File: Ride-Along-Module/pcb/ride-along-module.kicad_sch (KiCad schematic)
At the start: 7 parts

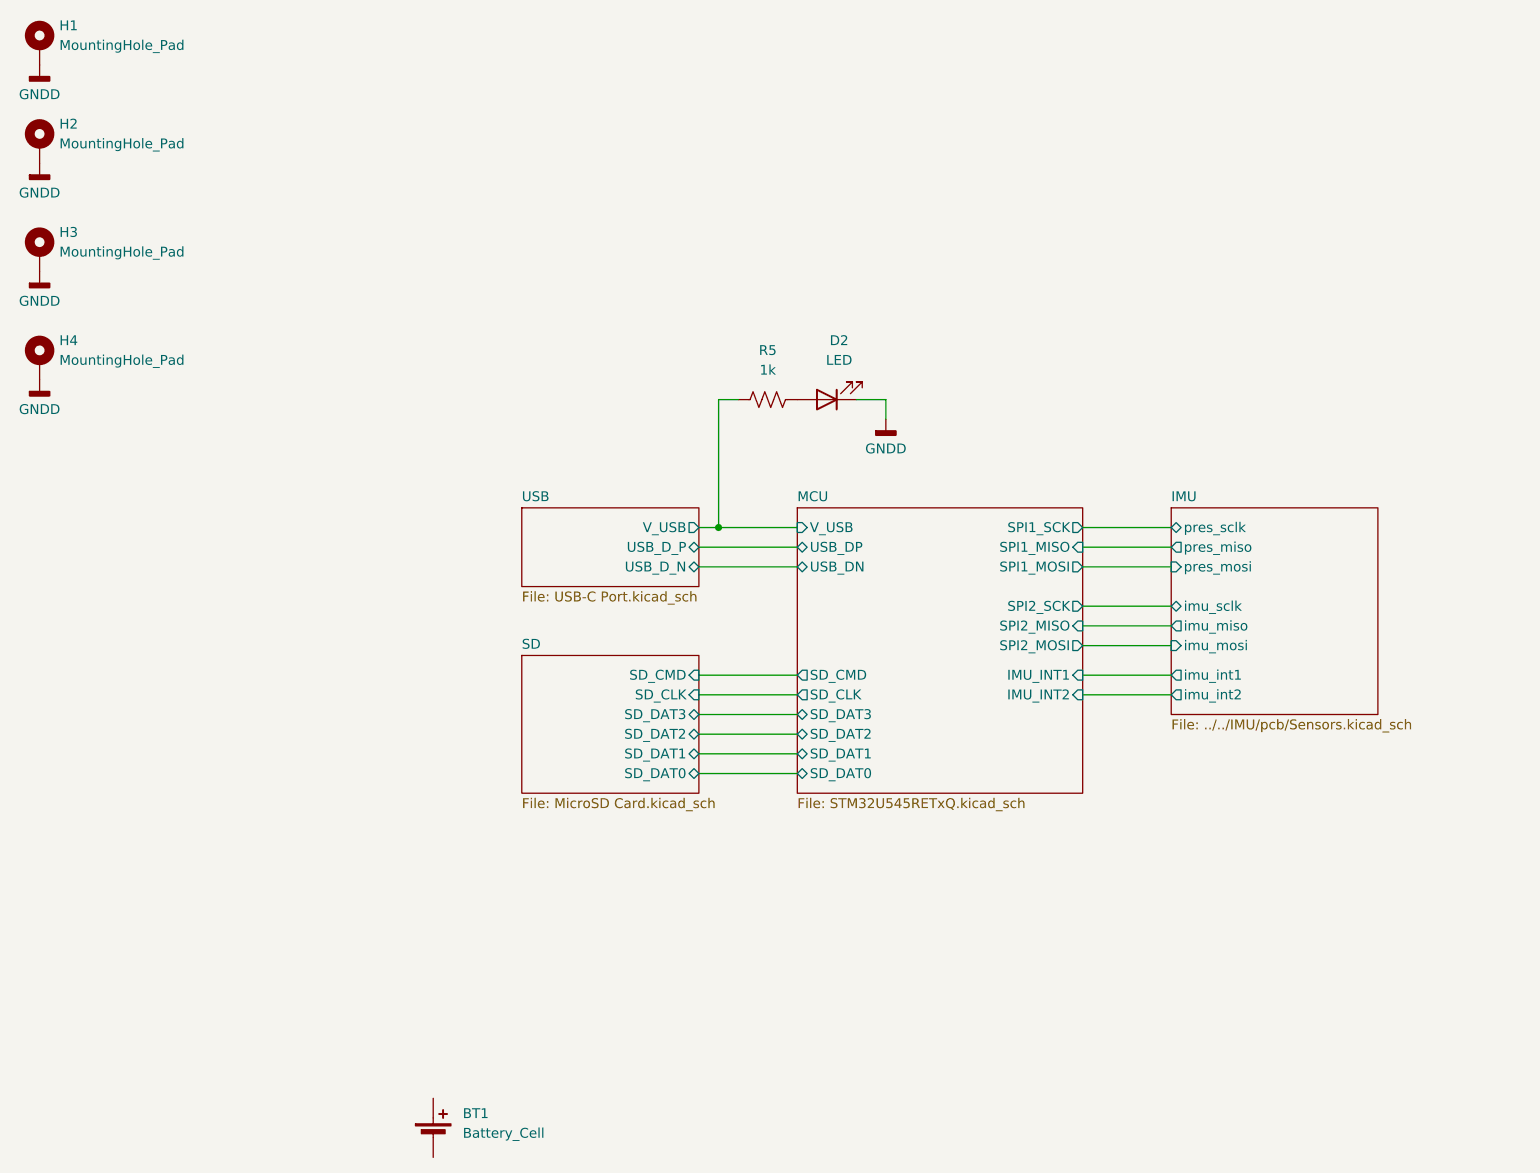
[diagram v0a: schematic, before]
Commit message: More reuse blocks. Added battery circuit to ride along board
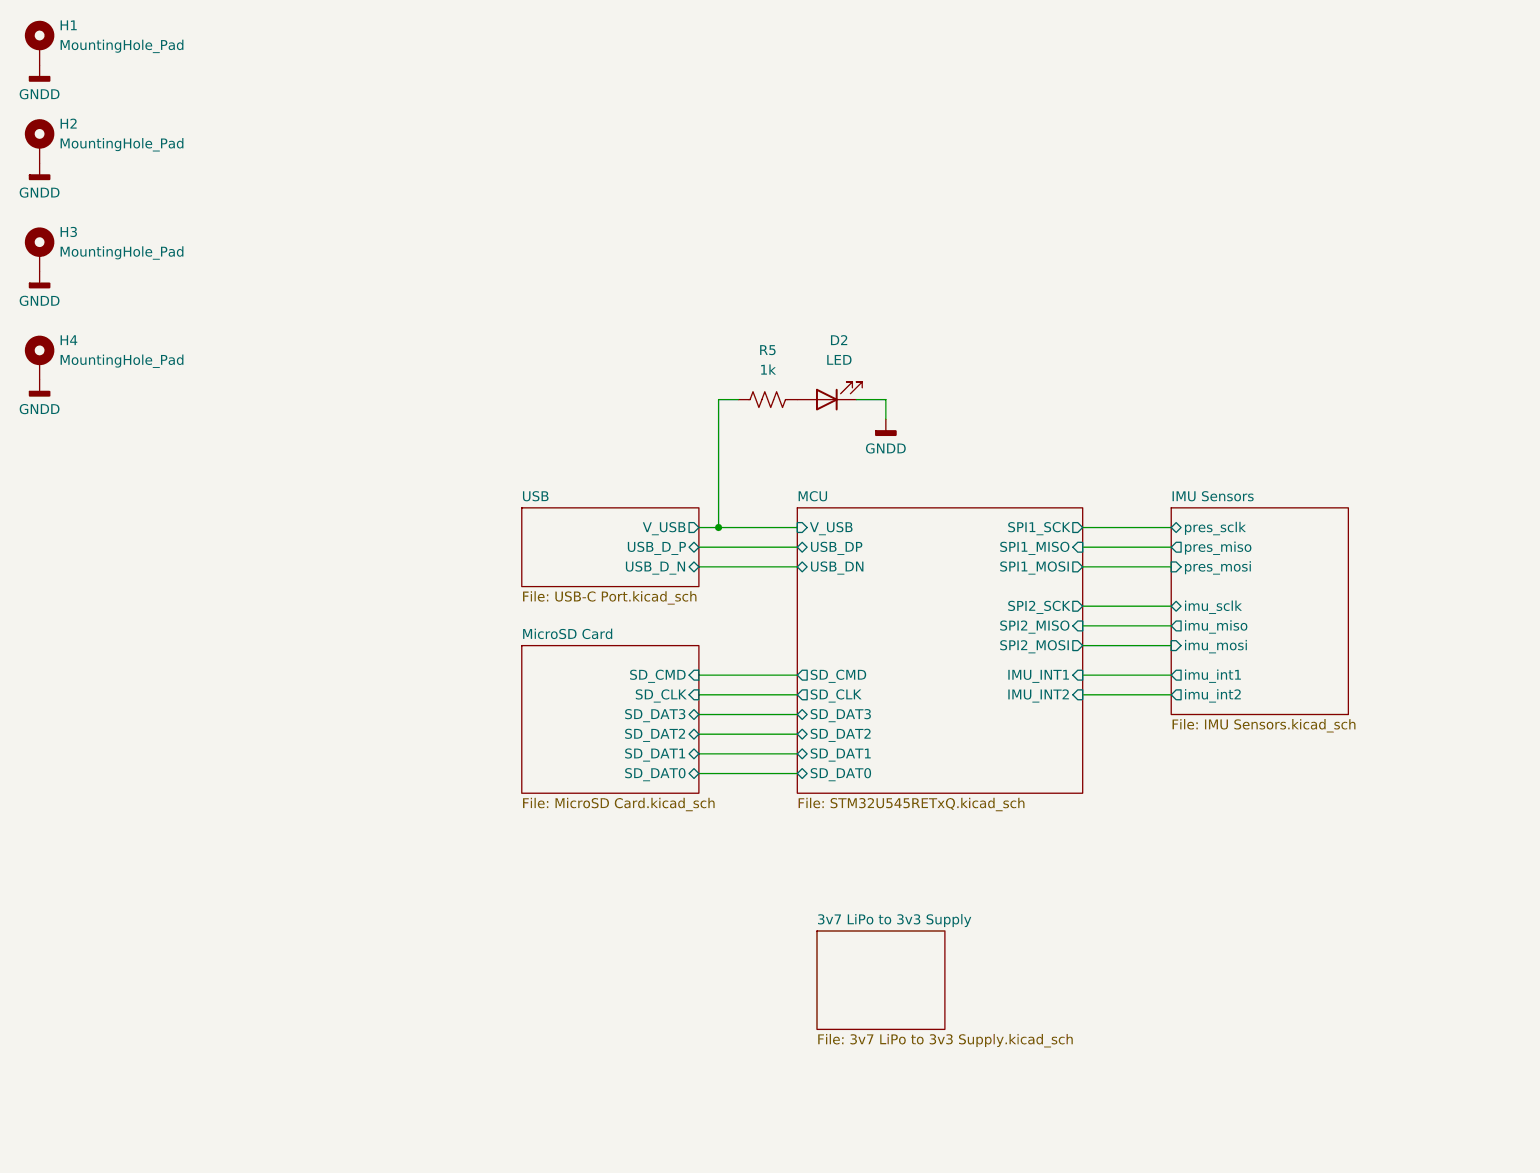
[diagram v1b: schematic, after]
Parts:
- removed BT1: Battery_Cell, Connector_JST:JST_PH_B2B-PH-K_1x02_P2.00mm_Vertical, symbol Device:Battery_Cell
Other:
- removed sheet IMU
- removed sheet SD
- added sheet 3v7 LiPo to 3v3 Supply (3v7 LiPo to 3v3 Supply.kicad_sch)
- added sheet IMU Sensors (IMU Sensors.kicad_sch)
- added sheet MicroSD Card (MicroSD Card.kicad_sch)

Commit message: Ride-Along Module Rev. 1
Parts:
- added FID1, FID2, FID3: Fiducial, Fiducial:Fiducial_1mm_Mask3mm, symbol Mechanical:Fiducial
- D1: renamed from D2; footprint LED_SMD:LED_0603_1608Metric_Pad1.05x0.95mm_HandSolder -> LED_SMD:LED_0603_1608Metric
- R1: renamed from R5; footprint Resistor_SMD:R_0603_1608Metric_Pad0.98x0.95mm_HandSolder -> Resistor_SMD:R_0603_1608Metric
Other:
- sheet IMU Sensors ports: added imu_cs, pres_cs; removed none
- sheet MCU ports: added imu_cs, pres_cs; removed none
- company: (none) -> Rowan Rocketry
- title: (none) -> Ride-Along Module
